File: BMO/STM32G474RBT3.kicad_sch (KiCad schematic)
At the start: 0 parts

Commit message: update pcb
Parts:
- added C10, C11, C12, C14, C22, C34: 100n, Capacitor_SMD:C_0402_1005Metric, symbol Device:C_Small
- added C13: 10n, Capacitor_SMD:C_0603_1608Metric, symbol Device:C_Small
- added C15, C16: 10p, Capacitor_SMD:C_0402_1005Metric, symbol Device:C_Small
- added C9: 4u7, Capacitor_SMD:C_0603_1608Metric, symbol Device:C_Small
- added H1, H2, H3, H4: MountingHole_Pad, MountingHole:MountingHole_3.2mm_M3_Pad_Via, symbol Mechanical:MountingHole_Pad
- added J11: Conn_ST_STDC14, Connector_PinHeader_1.27mm:PinHeader_2x07_P1.27mm_Vertical_SMD, symbol Connector:Conn_ST_STDC14
- added L2: 39n, Inductor_SMD:L_0603_1608Metric, symbol Device:L_Small
- added R1, R2: 2k2, Resistor_SMD:R_0603_1608Metric, symbol Device:R_Small
- added R3, R4, R5, R6: 4k7, Resistor_SMD:R_0603_1608Metric, symbol Device:R_Small
- added SW1: SW_Push, KiCad:SW Push 1P1T NO 6x6mm H9.5mm, symbol Switch:SW_Push
- added U1: STM32G474RBTx, Package_QFP:LQFP-64_10x10mm_P0.5mm, symbol MCU_ST_STM32G4:STM32G474RBTx
- added Y2: 16MHz, Crystal:Crystal_SMD_EuroQuartz_MT-4Pin_3.2x2.5mm, symbol Device:Crystal_GND24_Small
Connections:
- new net: C15.1, U1.5 (PF0), Y2.4
- new net: C13.2, L2.2, U1.29 (VDDA)
- new net: C16.1, U1.6 (PF1), Y2.2
- new net +3.3V: C10.2, C11.2, C12.2, C22.2, C34.2, C9.2, J11.3 (VCC), L2.1, R1.1, R2.1, R3.1, R4.1, R5.1, R6.1, U1.1 (VBAT), U1.16 (VDD), U1.28 (VREF+), U1.32 (VDD), U1.48 (VDD), U1.64 (VDD)
- new net BLE_USART3_RX: U1.53 (PC11)
- new net BLE_USART3_TX: U1.52 (PC10)
- new net BUZZER: U1.34 (PB12)
- new net ENC_L_A_TIM2_CH1: U1.12 (PA0)
- new net ENC_L_B_TIM2_CH2: U1.13 (PA1)
- new net ENC_R_A_TIM4_CH1: U1.59 (PB6)
- new net ENC_R_B_TIM4_CH2: U1.60 (PB7)
- new net GND: C10.1, C11.1, C12.1, C13.1, C14.2, C15.2, C16.2, C22.1, C34.1, C9.1, H1.1, H2.1, H3.1, H4.1, J11.11 (GNDDetect), J11.5 (GND), J11.7 (GND), SW1.2, U1.15 (VSS), U1.27 (VSSA), U1.31 (VSS), U1.47 (VSS), U1.63 (VSS), Y2.1, Y2.3
- new net I2C1_SCL_MPU-6050 & Jauge: R3.2, U1.51 (PA15)
- new net I2C1_SDA_MPU-6050 & Jauge: R4.2, U1.62 (PB9)
- new net I2C2_SCL_OLED: R2.2, U1.43 (PA9)
- new net I2C2_SDA_OLED: R1.2, U1.42 (PA8)
- new net I2C3_SCL_ToF_TCS: R5.2, U1.40 (PC8)
- new net I2C3_SDA_ToF_TCS: R6.2, U1.41 (PC9)
- new net LED_SPOT: U1.39 (PC7)
- new net LED_STATUS: U1.19 (PA5)
- new net LIDARX2__USART1_RX: U1.23 (PC5)
- new net LIDAR_M_CTR_TIM15_CH1: U1.36 (PB14)
- new net MOT_L_IN1_TIM3_CH1: U1.20 (PA6)
- new net MOT_L_IN2_TIM3_CH2: U1.21 (PA7)
- new net MOT_R_IN1_TIM3_CH3: U1.24 (PB0)
- new net MOT_R_IN2_TIM3_CH4: U1.25 (PB1)
- new net NRST: C14.1, J11.12 (~{RST}), SW1.1, U1.7 (PG10)
- new net SERVO_PINCE_TIM8_CH1: U1.38 (PC6)
- new net SWCLK: J11.6 (JCLK/SWCLK), U1.50 (PA14)
- new net SWDIO: J11.4 (JTMS/SWDIO), U1.49 (PA13)
- new net USER_Bouton: U1.2 (PC13)
- new net VCP_RX: J11.13 (VCP_RX), U1.17 (PA3)
- new net VCP_TX: J11.14 (VCP_TX), U1.14 (PA2)
- new net XSHUT_TOF1: U1.10 (PC2)
- new net XSHUT_TOF2: U1.11 (PC3)
- no-connect marks 0 -> 4
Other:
- note added: "OSC_IN"
- note added: "OSC_OUT"
- note added: "STLink/SWD Connector"
- note added: "STM32G474RBTx"

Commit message: Update sensor and MCU files
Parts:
- removed SW1: SW_Push, KiCad:SW Push 1P1T NO 6x6mm H9.5mm, symbol Switch:SW_Push
- added SW2: SW_Push, KiCad:SW Push 1P1T NO 6x6mm H9.5mm, symbol Switch:SW_Push
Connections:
- net GND: now also SW2.2
- net NRST: now also SW2.1
- net BUZZER: no longer names the net of U1.34 (PB12)
- net LED_SPOT: no longer names the net of U1.39 (PC7)
- net LED_STATUS: no longer names the net of U1.19 (PA5)
- no-connect marks 4 -> 23
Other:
- note added: "Reset Bouton"
- moved on the sheet: H1, H2, H3, H4, J11, R1, R2, R3, R4, R6

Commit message: Update PCB modifications
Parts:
- added C11, C12: 1u, Capacitor_SMD:C_0402_1005Metric, symbol Device:C_Small
- added D1: GREEN, LED_SMD:LED_0603_1608Metric, symbol Device:LED
- added J1: EXT, Connector_PinHeader_2.54mm:PinHeader_1x10_P2.54mm_Vertical, symbol Connector_Generic:Conn_01x10
- added R7: 1k, Resistor_SMD:R_0402_1005Metric, symbol Device:R_Small
- added R8: 10k, Resistor_SMD:R_0402_1005Metric, symbol Device:R_Small
- added SW1: USER, Button_Switch_SMD:SW_Push_1P1T_NO_CK_KMR2, symbol Switch:SW_Push
- C1: renamed from C15; JLCPCB Part # (none) -> C32949
- C10: renamed from C13; JLCPCB Part # (none) -> C57112
- C2: renamed from C16; JLCPCB Part # (none) -> C32949
- C3: renamed from C22; JLCPCB Part # (none) -> C1525
- C4: renamed from C34; JLCPCB Part # (none) -> C1525
- C5: renamed from C14; JLCPCB Part # (none) -> C1525
- C6: renamed from C9; JLCPCB Part # (none) -> C19666
- C7: renamed from C10; JLCPCB Part # (none) -> C1525
- C8: renamed from C11; JLCPCB Part # (none) -> C1525
- C9: renamed from C12; JLCPCB Part # (none) -> C1525
- J2: renamed from J11; JLCPCB Part # (none) -> C3975190
- L1: renamed from L2; JLCPCB Part # (none) -> C75654
- R1: renamed from R6; value 4k7 -> 2k2
- R2: renamed from R5; value 4k7 -> 2k2
- R3: renamed from R2; now not fitted
- R6: renamed from R1; now not fitted
- SW2: footprint KiCad:SW Push 1P1T NO 6x6mm H9.5mm -> Button_Switch_THT:SW_PUSH_6mm_H9.5mm
- U1: JLCPCB Part # (none) -> C1235414
- Y1: renamed from Y2; JLCPCB Part # (none) -> C13738
- renumbered R3 to R5
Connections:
- net +3.3V: now also J1.1 (Pin_1), SW1.1; no longer C3.2, U1.28 (VREF+)
- net GND: now also Y1.2 (G), Y1.4 (G), C11.2, C12.2, D1.1 (K), J1.10 (Pin_10), R8.2; no longer Y1.1, Y1.3
- net USER_Bouton: now also R8.1, SW1.2
- net at C1.1, U1.5 (PF0): now also Y1.3; no longer Y1.4
- net MOT_nSLEEP: now reaches U1.18 (PA4)
- net LED_STATUS: now reaches U1.19 (PA5)
- net LED_STATUS: now also R7.1
- net +3V3A: now reaches C10.2, L1.2, U1.29 (VDDA)
- net +3V3A: now also C3.2, U1.28 (VREF+), C11.1, C12.1
- net TOF2_INT: now reaches U1.3 (PC14)
- net TOF1_INT: now reaches U1.30 (PB10)
- net EXT_PB11: now reaches U1.33 (PB11)
- net EXT_PB11: now also J1.7 (Pin_7)
- net EXT_PB12: now reaches U1.34 (PB12)
- net EXT_PB12: now also J1.4 (Pin_4)
- net EXT_PB13: now reaches U1.35 (PB13)
- net EXT_PB13: now also J1.5 (Pin_5)
- net EXT_PB15: now reaches U1.37 (PB15)
- net EXT_PB15: now also J1.6 (Pin_6)
- net EXT_PC7: now reaches U1.39 (PC7)
- net EXT_PC7: now also J1.3 (Pin_3)
- net COLOR_INT: now reaches U1.4 (PC15)
- net BLE_En: now reaches U1.44 (PA10)
- net LIDAR_M_CTR_TIM16_CH1: now reaches U1.46 (PA12)
- net CHARGER_INT: now reaches U1.54 (PC12)
- net FG_GPOUT: now reaches U1.55 (PD2)
- net SWO: now reaches U1.56 (PB3)
- net SWO: now also J2.8 (JTDO/SWO)
- net MPU_INT: now reaches U1.57 (PB4)
- net MOT_nFAULT: now reaches U1.58 (PB5)
- net at C2.1, U1.6 (PF1): now also Y1.1; no longer Y1.2
- net I2C1_SCL_ Jauge: now reaches U1.61 (PB8)
- net I2C1_SCL_ Jauge: now also R5.2
- net EXT_PC0: now reaches U1.8 (PC0)
- net EXT_PC0: now also J1.8 (Pin_8)
- net EXT_PC1: now reaches U1.9 (PC1)
- net EXT_PC1: now also J1.9 (Pin_9)
- net I2C1_SCL_MPU-6050 & Jauge: no longer names the net of U1.51 (PA15)
- net I2C1_SCL_MPU-6050 & Jauge: no longer R5.2
- net I2C1_SDA_MPU-6050 & Jauge renamed I2C1_SDA_ Jauge
- net I2C3_SCL_ToF_TCS renamed I2C3_SCL_ToF_TCS_MPU
- net I2C3_SDA_ToF_TCS renamed I2C3_SDA_ToF_TCS_MPU
- net LIDAR_M_CTR_TIM15_CH1 renamed NEOPIXEL
- new net: D1.2 (A), R7.2
- new net +5V: J1.2 (Pin_2)
- no-connect marks 23 -> 6
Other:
- note added: "ADC : PB11, PB12, PB13, PB15, PC0, PC1"
- note added: "Batterie sur un i2c sensors sur un autre i2c ecran sur son propre i2c (OK)"
- note added: "Buzzer PB12, LED de pince PC7 : à câbler"
- note added: "JLCPCB Part #"
- note added: "RESET_Bouton"
- note added: "TODO : Ajouter nQON"
- note removed: "Reset Bouton"
- moved on the sheet: J2, R1, R2, R5, SW2

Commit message: Schéma prêt pour le PCB
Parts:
- removed R3, R6: 2k2, Resistor_SMD:R_0603_1608Metric, symbol Device:R_Small
- added R33, R34: 2k2, Resistor_SMD:R_0603_1608Metric, symbol Device:R_Small
- C1, C2: JLCPCB Part # C32949 -> C32949; LCSC (none) -> C32949
- C10: JLCPCB Part # C57112 -> C57112; LCSC (none) -> C57112
- C11, C12: JLCPCB Part # C52923 -> C52923; LCSC (none) -> C52923
- C3, C4, C5, C7, C8, C9: JLCPCB Part # C1525 -> C1525; LCSC (none) -> C1525
- C6: JLCPCB Part # C19666 -> C19666; LCSC (none) -> C19666
- D1: JLCPCB Part # C12624 -> C12624; LCSC (none) -> C12624
- J1: JLCPCB Part # (none) -> C492409; LCSC (none) -> C492409
- J2: JLCPCB Part # C3975190 -> C5307809; LCSC (none) -> C5307809
- L1: value 39n -> 600R@100MHz; symbol Device:L_Small -> Device:FerriteBead_Small; JLCPCB Part # C75654 -> C1002; LCSC (none) -> C1002
- R1, R2: JLCPCB Part # (none) -> C4190; LCSC (none) -> C4190
- R4, R5: JLCPCB Part # (none) -> C23162; LCSC (none) -> C23162; now not fitted
- R7: JLCPCB Part # (none) -> C11702; LCSC (none) -> C11702
- R8: JLCPCB Part # (none) -> C25744; LCSC (none) -> C25744
- SW1: JLCPCB Part # (none) -> C72443; LCSC (none) -> C72443
- SW2: footprint Button_Switch_THT:SW_PUSH_6mm_H9.5mm -> Button_Switch_SMD:SW_Push_1P1T_NO_CK_KMR2; JLCPCB Part # (none) -> C72443; LCSC (none) -> C72443
- U1: LCSC (none) -> C1235414
- Y1: footprint Crystal:Crystal_SMD_EuroQuartz_MT-4Pin_3.2x2.5mm -> Crystal:Crystal_SMD_3225-4Pin_3.2x2.5mm; LCSC (none) -> C13738
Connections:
- net +3.3V: now also R33.2, R34.2
- net I2C2_SCL_OLED: now also R33.1
- net I2C2_SDA_OLED: now also R34.1
- net I2C3_SCL_ToF_TCS_MPU: now also R1.2; no longer R2.2
- net I2C3_SDA_ToF_TCS_MPU: now also R2.2; no longer R1.2
- net PWR_Bouton: now reaches U1.45 (PA11)
- net I2C1_SCL_ Jauge renamed I2C1_SCL_Jauge
- net I2C1_SCL_Jauge: now also R4.2; no longer R5.2
- net I2C1_SDA_ Jauge renamed I2C1_SDA_Jauge
- net I2C1_SDA_Jauge: now also R5.2; no longer R4.2
- no-connect marks 6 -> 5
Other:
- note removed: "Batterie sur un i2c sensors sur un autre i2c ecran sur son propre i2c (OK)"
- note removed: "JLCPCB Part #"
- note removed: "TODO : Ajouter nQON"
- moved on the sheet: C1, C10, C2, C3, C4, C6, C7, C8, C9, D1, R7, R8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

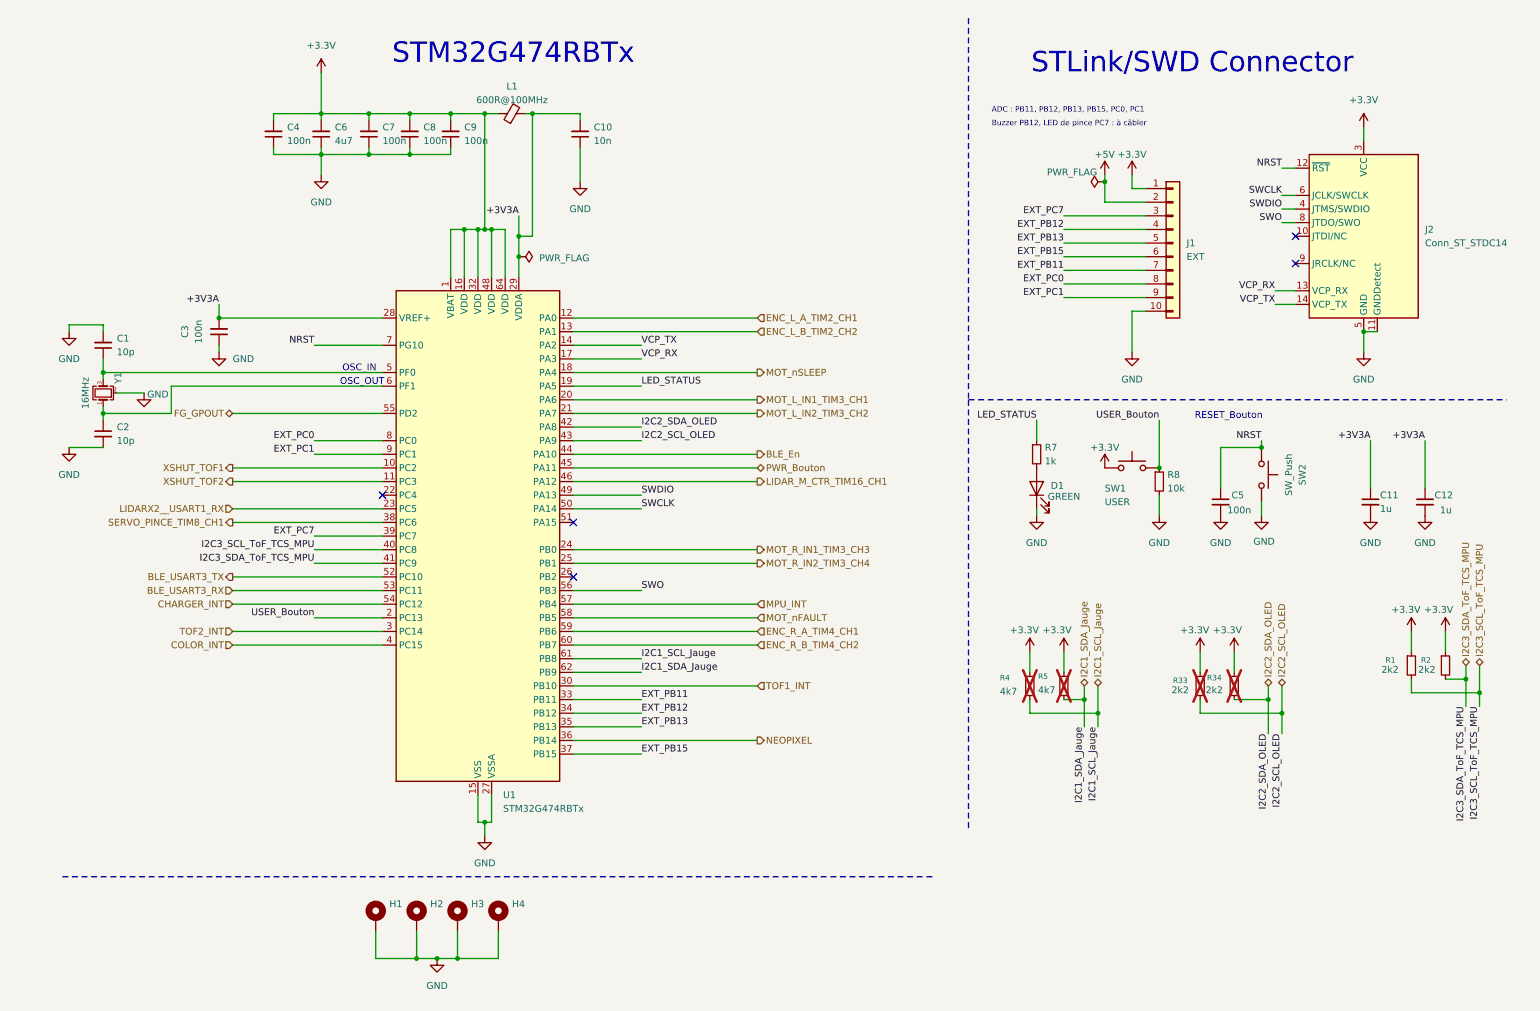
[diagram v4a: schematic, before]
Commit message: pcb(layout): finalize placement post-review and initiate routing
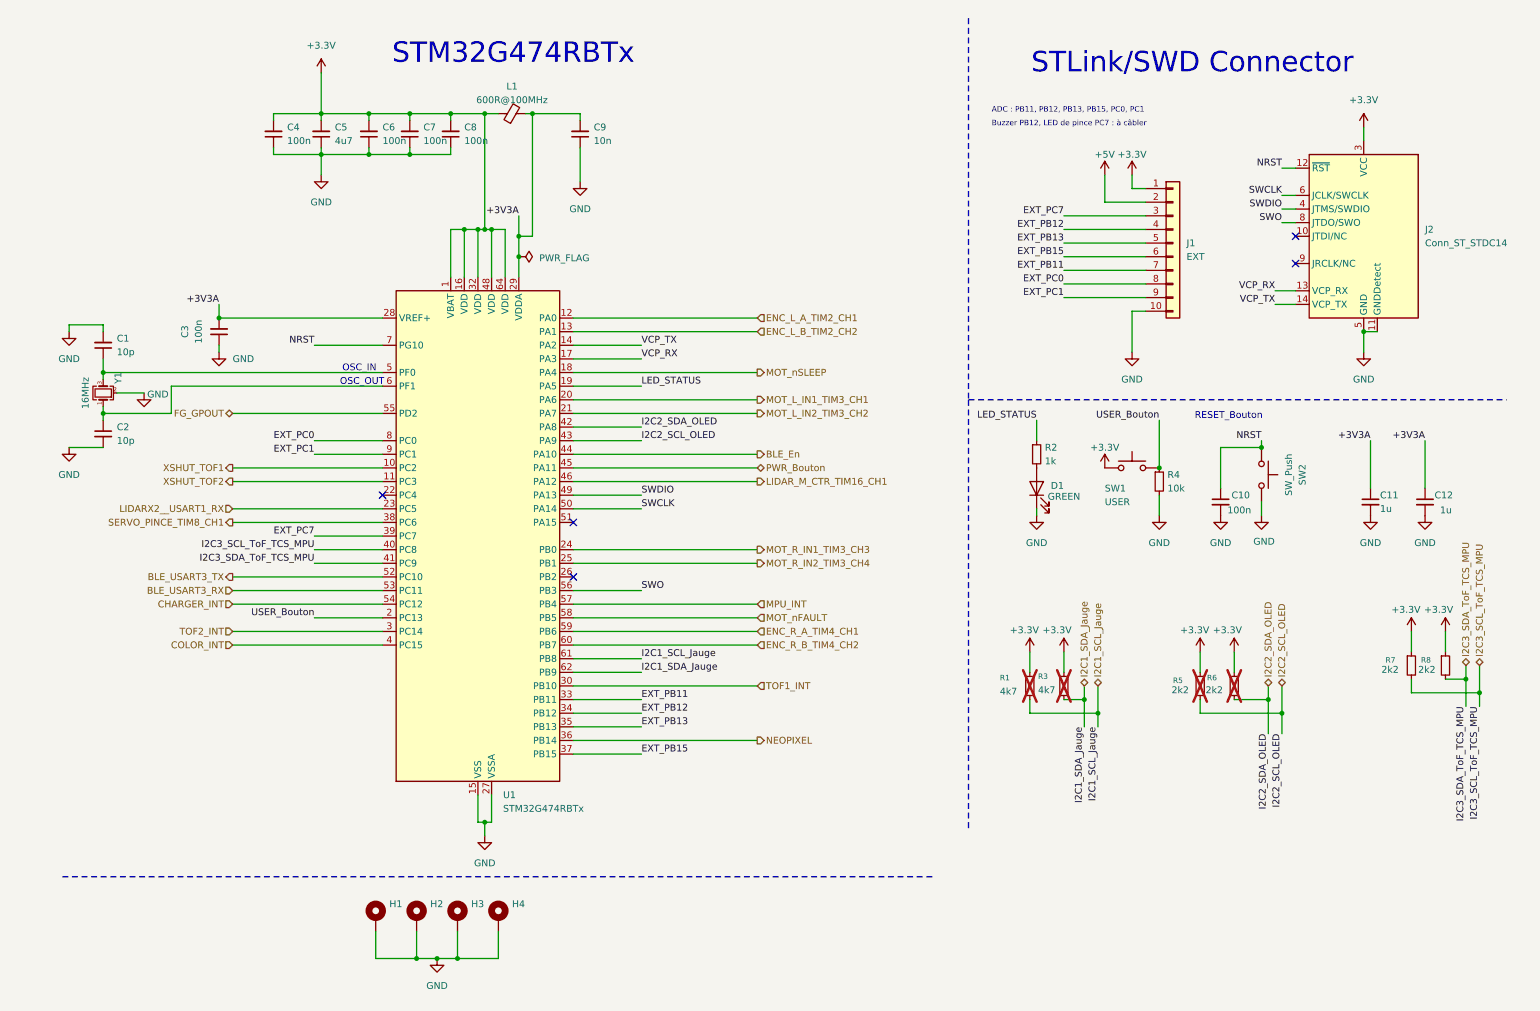
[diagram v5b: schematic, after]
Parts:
- renumbered C5 to C10, C6 to C5, C7 to C6, C8 to C7, C9 to C8, C10 to C9, R4 to R1, R7 to R2, R5 to R3, R8 to R4, R33 to R5, R34 to R6, R1 to R7, R2 to R8

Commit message: Mise à jour des fichiers PCB
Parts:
- added C45: 100n, Capacitor_SMD:C_0402_1005Metric, symbol Device:C_Small
- added TP10: TestPoint, TestPoint:TestPoint_Pad_D1.5mm, symbol Connector:TestPoint
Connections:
- net +3.3V: now also C45.2
- net +3V3A: now also TP10.1
- net GND: now also C45.1
- net MOT_nFAULT: now also U1.8 (PC0); no longer U1.58 (PB5)
- net EXT_PC0 renamed BUZZER_TIM17_CH1
- net BUZZER_TIM17_CH1: now also U1.58 (PB5); no longer U1.8 (PC0)
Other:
- note added: "ADC : PB11, PB12, PB13, PB15, PC1"
- note added: "Buzzer PB5 (TIM17_CH1) sur J1 broche 8, LED de pince PC7 : à câbler"
- note removed: "ADC : PB11, PB12, PB13, PB15, PC0, PC1"
- note removed: "Buzzer PB12, LED de pince PC7 : à câbler"

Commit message: feat(pcb): update placement, fallback I2C, and route MCU, sensors, and external pins
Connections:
- net BUZZER_TIM17_CH1: now also J1.9 (Pin_9); no longer J1.8 (Pin_8)
- net EXT_PB11: now also J1.8 (Pin_8); no longer J1.7 (Pin_7)
- net EXT_PB12: now also J1.7 (Pin_7); no longer J1.4 (Pin_4)
- net EXT_PB13: now also J1.6 (Pin_6); no longer J1.5 (Pin_5)
- net EXT_PB15: now also J1.5 (Pin_5); no longer J1.6 (Pin_6)
- net I2C3_SCL_ToF_TCS_MPU: now also J1.4 (Pin_4)
- net I2C3_SDA_ToF_TCS_MPU: now also J1.3 (Pin_3)
- net EXT_PC1: no longer names the net of U1.9 (PC1)
- net EXT_PC1: no longer J1.9 (Pin_9)
- net EXT_PC7: no longer names the net of U1.39 (PC7)
- net EXT_PC7: no longer J1.3 (Pin_3)
- no-connect marks 5 -> 7
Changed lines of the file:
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@@
 		(at 109.22 118.11)
 	)
+	(no_connect
+		(at 73.66 110.49)
+	)
+	(no_connect
+		(at 73.66 95.25)
+	)
 	(wire
 		(pts
@@
 	(wire
 		(pts
-			(xy 60.96 95.25) (xy 73.66 95.25)
-		)
-		(stroke
-			(width 0)
-			(type default)
-		)
-	)
-	(wire
-		(pts
 			(xy 88.9 53.34) (xy 88.9 62.23)
 		)
@@
 			(width 0)
 			(type default)
-		)
-	)
-	(wire
-		(pts
-			(xy 60.96 110.49) (xy 73.66 110.49)
-		)
-		(stroke
-			(width 0)
-			(type default)
-		)
-	)
-	(label "EXT_PB12"
-		(at 200.66 53.34 180)
-		(effects
-			(font
-				(size 1.27 1.27)
-			)
-			(justify right bottom)
-		)
-	)
-	(label "BUZZER_TIM17_CH1"
-		(at 200.66 63.5 180)
-		(effects
-			(font
-				(size 1.27 1.27)
-			)
-			(justify right bottom)
 		)
 	)
@@
 		)
 	)
-	(label "EXT_PB15"
-		(at 200.66 58.42 180)
-		(effects
-			(font
-				(size 1.27 1.27)
-			)
-			(justify right bottom)
-		)
-	)
 	(label "EXT_PB11"
 		(at 121.92 140.97 0)
@@
 		)
 	)
-	(label "EXT_PC7"
-		(at 60.96 110.49 180)
-		(effects
-			(font
-				(size 1.27 1.27)
-			)
-			(justify right bottom)
-		)
-	)
 	(label "VCP_RX"
 		(at 240.03 64.77 180)
@@
 		)
 	)
-	(label "EXT_PB11"
-		(at 200.66 60.96 180)
-		(effects
-			(font
-				(size 1.27 1.27)
-			)
-			(justify right bottom)
-		)
-	)
 	(label "SWO"
 		(at 241.3 52.07 180)
@@
 		)
 	)
+	(label "EXT_PB15"
+		(at 200.66 55.88 180)
+		(effects
+			(font
+				(size 1.27 1.27)
+			)
+			(justify right bottom)
+		)
+	)
 	(label "SWCLK"
 		(at 241.3 46.99 180)
@@
 		)
 	)
+	(label "EXT_PB11"
+		(at 200.66 63.5 180)
+		(effects
+			(font
+				(size 1.27 1.27)
+			)
+			(justify right bottom)
+		)
+	)
 	(label "I2C2_SCL_OLED"
 		(at 241.3 147.32 270)
@@
 		)
 	)
-	(label "EXT_PC7"
-		(at 200.66 50.8 180)
+	(label "EXT_PB13"
+		(at 200.66 58.42 180)
 		(effects
 			(font
@@
 		)
 	)
-	(label "EXT_PC1"
-		(at 200.66 66.04 180)
-		(effects
-			(font
-				(size 1.27 1.27)
-			)
-			(justify right bottom)
-		)
-	)
 	(label "BUZZER_TIM17_CH1"
 		(at 143.51 125.73 0)
@@
 		)
 	)
-	(label "EXT_PB13"
-		(at 200.66 55.88 180)
+	(label "I2C3_SDA_ToF_TCS_MPU"
+		(at 200.66 50.8 180)
 		(effects
 			(font
@@
 		)
 	)
+	(label "I2C3_SCL_ToF_TCS_MPU"
+		(at 200.66 53.34 180)
+		(effects
+			(font
+				(size 1.27 1.27)
+			)
+			(justify right bottom)
+		)
+	)
 	(label "VCP_TX"
 		(at 240.03 67.31 180)
@@
 		)
 	)
+	(label "EXT_PB12"
+		(at 200.66 60.96 180)
+		(effects
+			(font
+				(size 1.27 1.27)
+			)
+			(justify right bottom)
+		)
+	)
 	(label "I2C1_SCL_Jauge"
 		(at 121.92 133.35 0)
@@
 		)
 	)
+	(label "BUZZER_TIM17_CH1"
+		(at 200.66 66.04 180)
+		(effects
+			(font
+				(size 1.27 1.27)
+			)
+			(justify right bottom)
+		)
+	)
 	(label "SWO"
 		(at 121.92 120.65 0)
@@
 		)
 	)
-	(label "EXT_PC1"
-		(at 60.96 95.25 180)
-		(effects
-			(font
-				(size 1.27 1.27)
-			)
-			(justify right bottom)
-		)
-	)

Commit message: updated the shematic and routed the pcb
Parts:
- R1, R3: now fitted
- R7, R8: now not fitted
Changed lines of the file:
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@@
 		(on_board yes)
 		(in_pos_files yes)
-		(dnp yes)
+		(dnp no)
 		(property "Reference" "R1"
 			(at 188.722 136.906 0)
@@
 		(on_board yes)
 		(in_pos_files yes)
-		(dnp no)
+		(dnp yes)
 		(property "Reference" "R8"
 			(at 267.208 133.604 0)
@@
 		(on_board yes)
 		(in_pos_files yes)
-		(dnp no)
+		(dnp yes)
 		(property "Reference" "R7"
 			(at 260.604 133.604 0)
@@
 		(on_board yes)
 		(in_pos_files yes)
-		(dnp yes)
+		(dnp no)
 		(property "Reference" "R3"
 			(at 195.834 136.652 0)
